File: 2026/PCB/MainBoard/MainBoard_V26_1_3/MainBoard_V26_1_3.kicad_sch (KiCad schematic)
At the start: 93 parts, among them J1 Raspberry_Pi_2_3, J13 //Drib, J15 TFT3, J16 CAN_CON, J2 fan, J3 MOLEX, J5 Conn_01x05_Socket, J6 Debug, Q1 Q_NMOS_GSD, Q2 Q_NMOS_GSD, SW1 SW_MEC_5E, SW2 Ras_1, SW3 Ras_2, SW4 SW_Wuerth_450301014042, SW5 SW_MEC_5E, SW6 SW_MEC_5E, U1 STM32F446RETx, U10 MPU9250, U2 LMR51460FSQDRRRQ1, U3 MOUDLE-SEEEDUINO-XIAO, U5 MCP1703AT-3302E/CB, U6 BNO055, U7 LTC4451AV-TRPBF, U8 MAX3051, Y1 CSTNE16M0V530000R0

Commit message: V3回路完成
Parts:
- removed R8, R9: 2.2k, Resistor_SMD:R_0603_1608Metric_Pad0.98x0.95mm_HandSolder, symbol Device:R
- removed SW4: SW_Wuerth_450301014042, 0_Library:slideSW, symbol Switch:SW_Wuerth_450301014042
- removed SW5, SW6: SW_MEC_5E, 0_Library:SW_SKRPACE010, symbol Switch:SW_MEC_5E
- removed U10: MPU9250, Connector_PinHeader_2.54mm:PinHeader_1x10_P2.54mm_Vertical, symbol MainBoard:MPU9250
- removed U6: BNO055, Connector_PinHeader_2.54mm:PinHeader_1x04_P2.54mm_Vertical, symbol MainBoard:BNO055
- added C26, C27, C28: 0.1u, Capacitor_SMD:C_0603_1608Metric_Pad1.08x0.95mm_HandSolder, symbol Device:C
- added U6: LSM6DSO32XTR, LGA_O32XTR_STM, symbol 2026-08-16_15-19-59:LSM6DSO32XTR
- added U9: LTC4451AV-TRPBF, 0_Library:05-08-1683_ADI, symbol 2026-06-14_01-17-08:LTC4451AV-TRPBF
- R1: value 10k -> 100k
- R10: value 4.7k -> 100k
- R11: value 1k -> 10k
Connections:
- net +3.3V: now also C27.2, C28.2, U6.5 (Vdd_IO), U6.8 (Vdd)
- net +5V: now also R1.2, C26.1, U9.2 (IN), U9.3 (IN), U9.4 (IN), U9.5 (IN), U9.6 (IN), U9.7 (IN); no longer C18.1, U5.3 (Vin), U7.1 (VCC)
- net GND: now also C26.2, C27.1, C28.1, U6.2 (SDx), U6.3 (SCx), U6.6 (GND), U6.7 (GND), U9.14 (GND); no longer R1.2
- net SPI1.CLK: now also U6.13 (SCL)
- net SPI1.CS: now also U6.12 (CS)
- net SPI1.MISO: now also U6.1 (SDO/SA0)
- net SPI1.MOSI: now also U6.14 (SDA)
- net SPI2.CS: now also U1.50 (PA15); no longer U1.28 (PB2)
- net at R1.1: now also U9.16 (SHDN#); no longer U1.60 (BOOT0)
- net I2C_SCL: no longer names the net of U1.58 (PB6)
- net I2C_SDA: no longer names the net of U1.59 (PB7)
- net discharge: no longer names the net of U1.57 (PB5)
- net imu.reset: no longer names the net of U1.39 (PC8)
- new net 5V_For3.3V: C18.1, U5.3 (Vin), U9.10 (OUT), U9.11 (OUT), U9.12 (OUT), U9.13 (OUT), U9.8 (OUT), U9.9 (OUT)
- no-connect marks 29 -> 36
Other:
- moved on the sheet: J5

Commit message: 回路修正、PCB大枠決定
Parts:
- added R8: 10k, Resistor_SMD:R_0603_1608Metric_Pad0.98x0.95mm_HandSolder, symbol Device:R
- U6: footprint LGA_O32XTR_STM -> 0_Library:LGA_O32XTR_STM-M
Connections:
- net +3.3V: now also R8.2
- net LED1: now also U1.61 (PB8); no longer U1.33 (PB12)
- net SPI1.CS: now also U1.50 (PA15); no longer U1.24 (PC4)
- net SPI2.CS: now also U1.33 (PB12); no longer U1.50 (PA15)
- net ESTOP: now reaches J1.26 (~{CE1}/GPIO7)
- net ESTOP: now also U1.8 (PC0), R8.1
- no-connect marks 36 -> 35
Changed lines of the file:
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@@
 	)
 	(no_connect
-		(at 135.89 128.27)
+		(at 135.89 123.19)
 	)
 	(no_connect
@@
 	)
 	(no_connect
-		(at 129.54 320.04)
-	)
-	(no_connect
 		(at 129.54 337.82)
 	)
@@
 	)
 	(no_connect
+		(at 100.33 97.79)
+	)
+	(no_connect
 		(at 326.39 151.13)
 	)
@@
 	)
 	(no_connect
-		(at 100.33 87.63)
-	)
-	(no_connect
 		(at 100.33 69.85)
 	)
@@
 	(wire
 		(pts
+			(xy 187.96 91.44) (xy 187.96 93.98)
+		)
+		(stroke
+			(width 0)
+			(type default)
+		)
+	)
+	(wire
+		(pts
 			(xy 502.92 210.82) (xy 510.54 210.82)
 		)
@@
 	(wire
 		(pts
+			(xy 187.96 93.98) (xy 182.88 93.98)
+		)
+		(stroke
+			(width 0)
+			(type default)
+		)
+	)
+	(wire
+		(pts
 			(xy 118.11 151.13) (xy 119.38 151.13)
 		)
@@
 		)
 	)
+	(global_label "LED1"
+		(shape output)
+		(at 135.89 128.27 0)
+		(fields_autoplaced yes)
+		(effects
+			(font
+				(size 1.27 1.27)
+			)
+			(justify left)
+		)
+		(property "Intersheetrefs" "${INTERSHEET_REFS}"
+			(at 143.5318 128.27 0)
+			(effects
+				(font
+					(size 1.27 1.27)
+				)
+				(justify left)
+				(hide yes)
+			)
+		)
+	)
 	(global_label "SWDIO"
 		(shape input)
@@
 		)
 	)
-	(global_label "SPI2.CS"
-		(shape bidirectional)
-		(at 135.89 102.87 0)
-		(fields_autoplaced yes)
-		(effects
-			(font
-				(size 1.27 1.27)
-			)
-			(justify left)
-		)
-		(property "Intersheetrefs" "${INTERSHEET_REFS}"
-			(at 147.3646 102.87 0)
-			(effects
-				(font
-					(size 1.27 1.27)
-				)
-				(justify left)
-				(hide yes)
-			)
-		)
-	)
 	(global_label "MD4_TX"
 		(shape output)
@@
 		)
 	)
+	(global_label "ESTOP"
+		(shape bidirectional)
+		(at 129.54 320.04 0)
+		(fields_autoplaced yes)
+		(effects
+			(font
+				(size 1.27 1.27)
+			)
+			(justify left)
+		)
+		(property "Intersheetrefs" "${INTERSHEET_REFS}"
+			(at 139.5631 320.04 0)
+			(effects
+				(font
+					(size 1.27 1.27)
+				)
+				(justify left)
+				(hide yes)
+			)
+		)
+	)
+	(global_label "SPI2.CS"
+		(shape bidirectional)
+		(at 135.89 135.89 0)
+		(fields_autoplaced yes)
+		(effects
+			(font
+				(size 1.27 1.27)
+			)
+			(justify left)
+		)
+		(property "Intersheetrefs" "${INTERSHEET_REFS}"
+			(at 147.3646 135.89 0)
+			(effects
+				(font
+					(size 1.27 1.27)
+				)
+				(justify left)
+				(hide yes)
+			)
+		)
+	)
 	(global_label "SCK"
 		(shape bidirectional)
@@
 		)
 	)
+	(global_label "ESTOP"
+		(shape bidirectional)
+		(at 100.33 87.63 180)
+		(fields_autoplaced yes)
+		(effects
+			(font
+				(size 1.27 1.27)
+			)
+			(justify right)
+		)
+		(property "Intersheetrefs" "${INTERSHEET_REFS}"
+			(at 90.3069 87.63 0)
+			(effects
+				(font
+					(size 1.27 1.27)
+				)
+				(justify right)
+				(hide yes)
+			)
+		)
+	)
 	(global_label "UART5_TX_Dis"
 		(shape output)
@@
 		)
 	)
+	(global_label "ESTOP"
+		(shape bidirectional)
+		(at 175.26 93.98 180)
+		(fields_autoplaced yes)
+		(effects
+			(font
+				(size 1.27 1.27)
+			)
+			(justify right)
+		)
+		(property "Intersheetrefs" "${INTERSHEET_REFS}"
+			(at 165.2369 93.98 0)
+			(effects
+				(font
+					(size 1.27 1.27)
+				)
+				(justify right)
+				(hide yes)
+			)
+		)
+	)
 	(global_label "SW_RAS2"
 		(shape output)
@@
 		)
 	)
-	(global_label "LED1"
-		(shape output)
-		(at 135.89 135.89 0)
-		(fields_autoplaced yes)
-		(effects
-			(font
-				(size 1.27 1.27)
-			)
-			(justify left)
-		)
-		(property "Intersheetrefs" "${INTERSHEET_REFS}"
-			(at 143.5318 135.89 0)
-			(effects
-				(font
-					(size 1.27 1.27)
-				)
-				(justify left)
-				(hide yes)
-			)
-		)
-	)
 	(global_label "UART2_TX"
 		(shape output)
@@
 		)
 	)
+	(global_label "SPI1.CS"
+		(shape bidirectional)
+		(at 135.89 102.87 0)
+		(fields_autoplaced yes)
+		(effects
+			(font
+				(size 1.27 1.27)
+			)
+			(justify left)
+		)
+		(property "Intersheetrefs" "${INTERSHEET_REFS}"
+			(at 147.3646 102.87 0)
+			(effects
+				(font
+					(size 1.27 1.27)
+				)
+				(justify left)
+				(hide yes)
+			)
+		)
+	)
 	(global_label "LED2"
 		(shape output)
@@
 		)
 	)
-	(global_label "SPI1.CS"
-		(shape bidirectional)
-		(at 100.33 97.79 180)
-		(fields_autoplaced yes)
-		(effects
-			(font
-				(size 1.27 1.27)
-			)
-			(justify right)
-		)
-		(property "Intersheetrefs" "${INTERSHEET_REFS}"
-			(at 88.8554 97.79 0)
-			(effects
-				(font
-					(size 1.27 1.27)
-				)
-				(justify right)
-				(hide yes)
-			)
-		)
-	)
 	(global_label "CANL"
 		(shape bidirectional)
@@
 	)
 	(symbol
+		(lib_id "Device:R")
+		(at 179.07 93.98 90)
+		(unit 1)
+		(exclude_from_sim no)
+		(in_bom yes)
+		(on_board yes)
+		(dnp no)
+		(fields_autoplaced yes)
+		(property "Reference" "R8"
+			(at 179.07 87.63 90)
+			(effects
+				(font
+					(size 1.27 1.27)
+				)
+			)
+		)
+		(property "Value" "10k"
+			(at 179.07 90.17 90)
+			(effects
+				(font
+					(size 1.27 1.27)
+				)
+			)
+		)
+		(property "Footprint" "Resistor_SMD:R_0603_1608Metric_Pad0.98x0.95mm_HandSolder"
+			(at 179.07 95.758 90)
+			(effects
+				(font
+					(size 1.27 1.27)
+				)
+				(hide yes)
+			)
+		)
+		(property "Datasheet" "~"
+			(at 179.07 93.98 0)
+			(effects
+				(font
+					(size 1.27 1.27)
+				)
+				(hide yes)
+			)
+		)
+		(property "Description" "Resistor"
+			(at 179.07 93.98 0)
+			(effects
+				(font
+					(size 1.27 1.27)
+				)
+				(hide yes)
+			)
+		)
+		(pin "1"
+		)
+		(pin "2"
+		)
+		(instances
+			(project "MainBoard_V26_1_3"
+				(path "/1e41cf15-e032-452e-b093-2e98e4f5d157"
+					(reference "R8")
+					(unit 1)
+				)
+			)
+		)
+	)
+	(symbol
 		(lib_id "Switch:SW_Omron_B3FS")
 		(at 152.4 339.09 0)
@@
 	)
 	(symbol
+		(lib_id "power:+3.3V")
+		(at 187.96 91.44 0)
+		(unit 1)
+		(exclude_from_sim no)
+		(in_bom yes)
+		(on_board yes)
+		(dnp no)
+		(fields_autoplaced yes)
+		(property "Reference" "#PWR049"
+			(at 187.96 95.25 0)
+			(effects
+				(font
+					(size 1.27 1.27)
+				)
+				(hide yes)
+			)
+		)
+		(property "Value" "+3.3V"
+			(at 187.96 86.36 0)
+			(effects
+				(font
+					(size 1.27 1.27)
+				)
+			)
+		)
+		(property "Footprint" ""
+			(at 187.96 91.44 0)
+			(effects
+				(font
+					(size 1.27 1.27)
+				)
+				(hide yes)
+			)
+		)
+		(property "Datasheet" ""
+			(at 187.96 91.44 0)
+			(effects
+				(font
+					(size 1.27 1.27)
+				)
+				(hide yes)
+			)
+		)
+		(property "Description" ""
+			(at 187.96 91.44 0)
+			(effects
+				(font
+					(size 1.27 1.27)
+				)
+			)
+		)
+		(pin "1"
+		)
+		(instances
+			(project "MainBoard_V26_1_3"
+				(path "/1e41cf15-e032-452e-b093-2e98e4f5d157"
+					(reference "#PWR049")
+					(unit 1)
+				)
+			)
+		)
+	)
+	(symbol
 		(lib_id "MainBoard:MOUDLE-SEEEDUINO-XIAO")
 		(at 290.83 237.49 0)
@@
 			)
 		)
-		(property "Footprint" "LGA_O32XTR_STM"
+		(property "Footprint" "0_Library:LGA_O32XTR_STM-M"
 			(at 275.59 138.43 0)
 			(effects

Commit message: 基板外形、ESTOP変更、配置決定
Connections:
- net ESTOP: now also J1.37 (GPIO26); no longer J1.26 (~{CE1}/GPIO7)
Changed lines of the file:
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@@
 	)
 	(no_connect
-		(at 88.9 332.74)
+		(at 129.54 320.04)
 	)
 	(no_connect
@@
 		)
 	)
+	(global_label "ESTOP"
+		(shape bidirectional)
+		(at 88.9 332.74 180)
+		(fields_autoplaced yes)
+		(effects
+			(font
+				(size 1.27 1.27)
+			)
+			(justify right)
+		)
+		(property "Intersheetrefs" "${INTERSHEET_REFS}"
+			(at 78.8769 332.74 0)
+			(effects
+				(font
+					(size 1.27 1.27)
+				)
+				(justify right)
+				(hide yes)
+			)
+		)
+	)
 	(global_label "R3"
 		(shape input)
@@
 			(effects
 				(font
-					(size 1.27 1.27)
-				)
-				(justify left)
-				(hide yes)
-			)
-		)
-	)
-	(global_label "ESTOP"
-		(shape bidirectional)
-		(at 129.54 320.04 0)
-		(fields_autoplaced yes)
-		(effects
-			(font
-				(size 1.27 1.27)
-			)
-			(justify left)
-		)
-		(property "Intersheetrefs" "${INTERSHEET_REFS}"
-			(at 139.5631 320.04 0)
-			(effects
-				(font

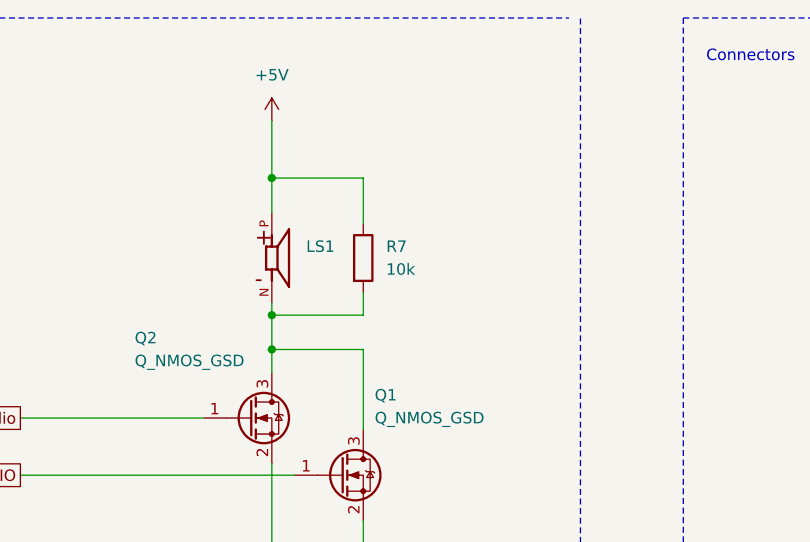
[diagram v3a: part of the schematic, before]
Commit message: 途中保存3、スピーカ抵抗変更
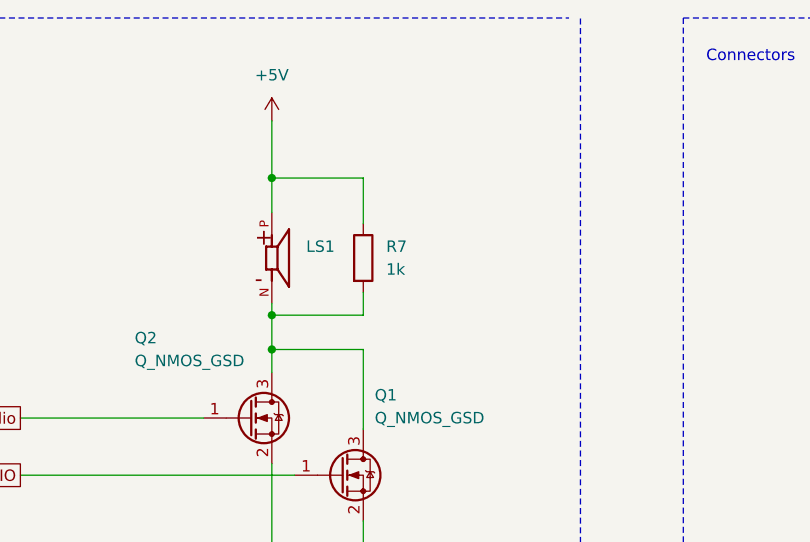
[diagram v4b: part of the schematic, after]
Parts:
- R7: value 10k -> 1k
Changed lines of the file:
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@@
 		(fields_autoplaced yes)
 		(property "Reference" "R7"
-			(at 425.45 52.07 0)
+			(at 425.45 52.0699 0)
 			(effects
 				(font
@@
 			)
 		)
-		(property "Value" "10k"
-			(at 425.45 54.61 0)
+		(property "Value" "1k"
+			(at 425.45 54.6099 0)
 			(effects
 				(font

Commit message: 途中保存6
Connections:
- net HEART_BEAT_LED: now also U1.55 (PB3); no longer U1.41 (PA8)
- net LED2: now also U1.57 (PB5); no longer U1.34 (PB13)
- net LED3: now also U1.58 (PB6); no longer U1.35 (PB14)
- net LED4: now also U1.59 (PB7); no longer U1.36 (PB15)
- no-connect marks 35 -> 36
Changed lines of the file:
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@@
 	)
 	(no_connect
-		(at 135.89 123.19)
-	)
-	(no_connect
 		(at 100.33 107.95)
 	)
 	(no_connect
-		(at 135.89 115.57)
-	)
-	(no_connect
 		(at 403.86 346.71)
 	)
@@
 	)
 	(no_connect
-		(at 135.89 120.65)
+		(at 135.89 143.51)
+	)
+	(no_connect
+		(at 135.89 85.09)
+	)
+	(no_connect
+		(at 135.89 138.43)
 	)
 	(no_connect
@@
 	)
 	(no_connect
+		(at 135.89 140.97)
+	)
+	(no_connect
 		(at 100.33 125.73)
 	)
@@
 	(global_label "LED4"
 		(shape output)
-		(at 135.89 143.51 0)
+		(at 135.89 125.73 0)
 		(fields_autoplaced yes)
 		(effects
@@
 		)
 		(property "Intersheetrefs" "${INTERSHEET_REFS}"
-			(at 143.5318 143.51 0)
+			(at 143.5318 125.73 0)
 			(effects
 				(font
@@
 		)
 	)
-	(global_label "HEART_BEAT_LED"
-		(shape output)
-		(at 135.89 85.09 0)
-		(fields_autoplaced yes)
-		(effects
-			(font
-				(size 1.27 1.27)
-			)
-			(justify left)
-		)
-		(property "Intersheetrefs" "${INTERSHEET_REFS}"
-			(at 154.0257 85.09 0)
-			(effects
-				(font
-					(size 1.27 1.27)
-				)
-				(justify left)
-				(hide yes)
-			)
-		)
-	)
 	(global_label "ESTOP"
 		(shape bidirectional)
@@
 		)
 	)
+	(global_label "LED3"
+		(shape output)
+		(at 135.89 123.19 0)
+		(fields_autoplaced yes)
+		(effects
+			(font
+				(size 1.27 1.27)
+			)
+			(justify left)
+		)
+		(property "Intersheetrefs" "${INTERSHEET_REFS}"
+			(at 143.5318 123.19 0)
+			(effects
+				(font
+					(size 1.27 1.27)
+				)
+				(justify left)
+				(hide yes)
+			)
+		)
+	)
 	(global_label "SPI2.CLK"
 		(shape bidirectional)
@@
 		)
 	)
-	(global_label "LED3"
-		(shape output)
-		(at 135.89 140.97 0)
-		(fields_autoplaced yes)
-		(effects
-			(font
-				(size 1.27 1.27)
-			)
-			(justify left)
-		)
-		(property "Intersheetrefs" "${INTERSHEET_REFS}"
-			(at 143.5318 140.97 0)
-			(effects
-				(font
-					(size 1.27 1.27)
-				)
-				(justify left)
-				(hide yes)
-			)
-		)
-	)
 	(global_label "SPI2.CS"
 		(shape bidirectional)
@@
 		)
 	)
+	(global_label "HEART_BEAT_LED"
+		(shape output)
+		(at 135.89 115.57 0)
+		(fields_autoplaced yes)
+		(effects
+			(font
+				(size 1.27 1.27)
+			)
+			(justify left)
+		)
+		(property "Intersheetrefs" "${INTERSHEET_REFS}"
+			(at 154.0257 115.57 0)
+			(effects
+				(font
+					(size 1.27 1.27)
+				)
+				(justify left)
+				(hide yes)
+			)
+		)
+	)
 	(global_label "UART4_RX"
 		(shape input)
@@
 		)
 	)
+	(global_label "LED2"
+		(shape output)
+		(at 135.89 120.65 0)
+		(fields_autoplaced yes)
+		(effects
+			(font
+				(size 1.27 1.27)
+			)
+			(justify left)
+		)
+		(property "Intersheetrefs" "${INTERSHEET_REFS}"
+			(at 143.5318 120.65 0)
+			(effects
+				(font
+					(size 1.27 1.27)
+				)
+				(justify left)
+				(hide yes)
+			)
+		)
+	)
 	(global_label "UART2_TX"
 		(shape output)
@@
 			(effects
 				(font
-					(size 1.27 1.27)
-				)
-				(justify left)
-				(hide yes)
-			)
-		)
-	)
-	(global_label "LED2"
-		(shape output)
-		(at 135.89 138.43 0)
-		(fields_autoplaced yes)
-		(effects
-			(font
-				(size 1.27 1.27)
-			)
-			(justify left)
-		)
-		(property "Intersheetrefs" "${INTERSHEET_REFS}"
-			(at 143.5318 138.43 0)
-			(effects
-				(font

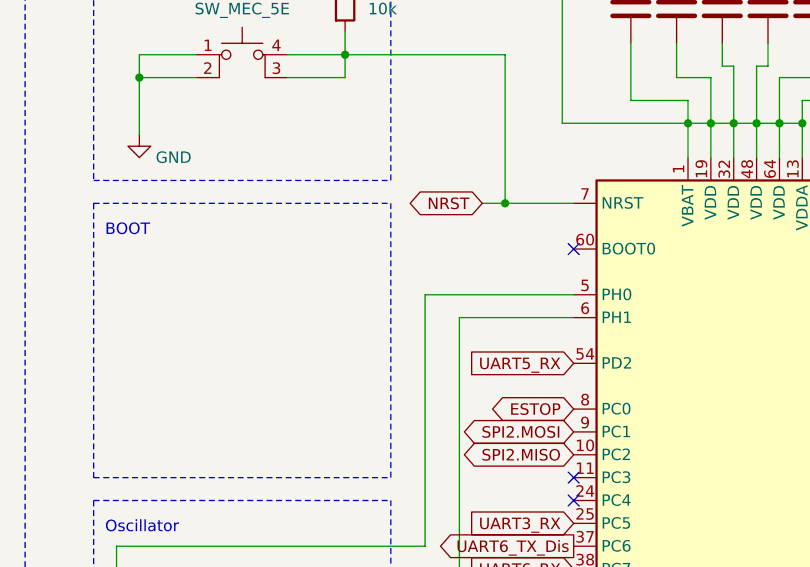
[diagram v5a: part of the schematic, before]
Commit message: BOOT0等修正
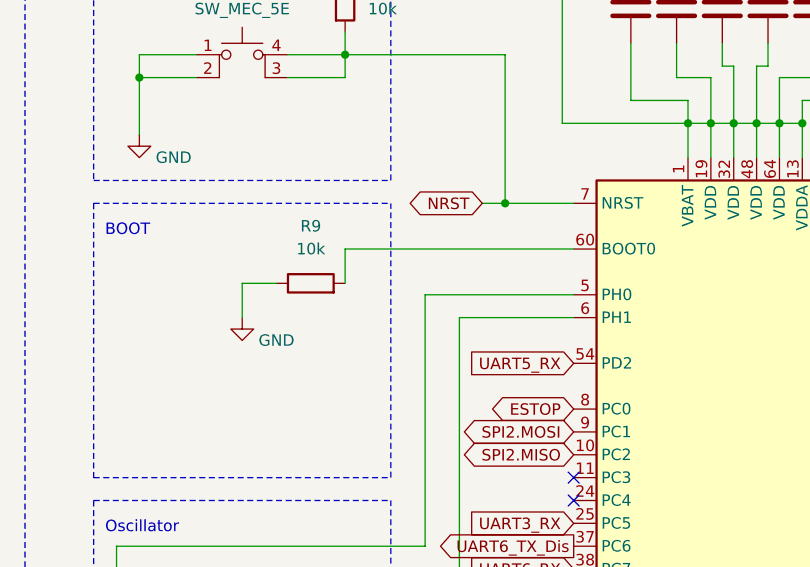
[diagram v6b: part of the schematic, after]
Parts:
- added R9: 10k, Resistor_SMD:R_0603_1608Metric_Pad0.98x0.95mm_HandSolder, symbol Device:R
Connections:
- net GND: now also R9.1
- net at U1.60 (BOOT0): now also R9.2
- no-connect marks 36 -> 35
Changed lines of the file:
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@@
 	)
 	(no_connect
-		(at 100.33 69.85)
-	)
-	(no_connect
 		(at 88.9 314.96)
 	)
@@
 	(wire
 		(pts
+			(xy 63.5 73.66) (xy 67.31 73.66)
+		)
+		(stroke
+			(width 0)
+			(type default)
+		)
+	)
+	(wire
+		(pts
 			(xy 411.48 351.79) (xy 411.48 349.25)
 		)
@@
 	(wire
 		(pts
+			(xy 63.5 77.47) (xy 63.5 73.66)
+		)
+		(stroke
+			(width 0)
+			(type default)
+		)
+	)
+	(wire
+		(pts
 			(xy 541.02 198.12) (xy 541.02 199.39)
 		)
@@
 	(wire
 		(pts
+			(xy 74.93 69.85) (xy 74.93 73.66)
+		)
+		(stroke
+			(width 0)
+			(type default)
+		)
+	)
+	(wire
+		(pts
 			(xy 40.64 229.87) (xy 43.18 229.87)
 		)
@@
 	(wire
 		(pts
+			(xy 100.33 69.85) (xy 74.93 69.85)
+		)
+		(stroke
+			(width 0)
+			(type default)
+		)
+	)
+	(wire
+		(pts
 			(xy 209.55 57.15) (xy 218.44 57.15)
 		)
@@
 	)
 	(symbol
+		(lib_id "Device:R")
+		(at 71.12 73.66 90)
+		(unit 1)
+		(exclude_from_sim no)
+		(in_bom yes)
+		(on_board yes)
+		(dnp no)
+		(fields_autoplaced yes)
+		(property "Reference" "R9"
+			(at 71.12 67.31 90)
+			(effects
+				(font
+					(size 1.27 1.27)
+				)
+			)
+		)
+		(property "Value" "10k"
+			(at 71.12 69.85 90)
+			(effects
+				(font
+					(size 1.27 1.27)
+				)
+			)
+		)
+		(property "Footprint" "Resistor_SMD:R_0603_1608Metric_Pad0.98x0.95mm_HandSolder"
+			(at 71.12 75.438 90)
+			(effects
+				(font
+					(size 1.27 1.27)
+				)
+				(hide yes)
+			)
+		)
+		(property "Datasheet" "~"
+			(at 71.12 73.66 0)
+			(effects
+				(font
+					(size 1.27 1.27)
+				)
+				(hide yes)
+			)
+		)
+		(property "Description" ""
+			(at 71.12 73.66 0)
+			(effects
+				(font
+					(size 1.27 1.27)
+				)
+			)
+		)
+		(pin "1"
+		)
+		(pin "2"
+		)
+		(instances
+			(project "MainBoard_V26_1_3"
+				(path "/1e41cf15-e032-452e-b093-2e98e4f5d157"
+					(reference "R9")
+					(unit 1)
+				)
+			)
+		)
+	)
+	(symbol
 		(lib_id "Device:C")
 		(at 142.24 43.18 0)
@@
 					(unit 1)
 				)
+			)
+		)
+	)
+	(symbol
+		(lib_id "power:GND")
+		(at 63.5 77.47 0)
+		(unit 1)
+		(exclude_from_sim no)
+		(in_bom yes)
+		(on_board yes)
+		(dnp no)
+		(property "Reference" "#PWR050"
+			(at 63.5 83.82 0)
+			(effects
+				(font
+					(size 1.27 1.27)
+				)
+				(hide yes)
+			)
+		)
+		(property "Value" "GND"
+			(at 67.31 80.01 0)
+			(effects
+				(font
+					(size 1.27 1.27)
+				)
+			)
+		)
+		(property "Footprint" ""
+			(at 63.5 77.47 0)
+			(effects
+				(font
+					(size 1.27 1.27)
+				)
+				(hide yes)
+			)
+		)
+		(property "Datasheet" ""
+			(at 63.5 77.47 0)
+			(effects
+				(font
+					(size 1.27 1.27)
+				)
+				(hide yes)
+			)
+		)
+		(property "Description" ""
+			(at 63.5 77.47 0)
+			(effects
+				(font
+					(size 1.27 1.27)
+				)
+			)
+		)
+		(pin "1"
+		)
+		(instances
+			(project "MainBoard_V26_1_3"
+				(path "/1e41cf15-e032-452e-b093-2e98e4f5d157"
+					(reference "#PWR050")
+					(unit 1)
+				)
